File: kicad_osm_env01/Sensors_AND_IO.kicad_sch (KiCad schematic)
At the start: 64 parts, among them J4 Conn_01x08, J8 STX-3000, U10 ICS-43434, U11 HPP845E131R5, U12 MIC94073YC6, U3 VEML7700-TT

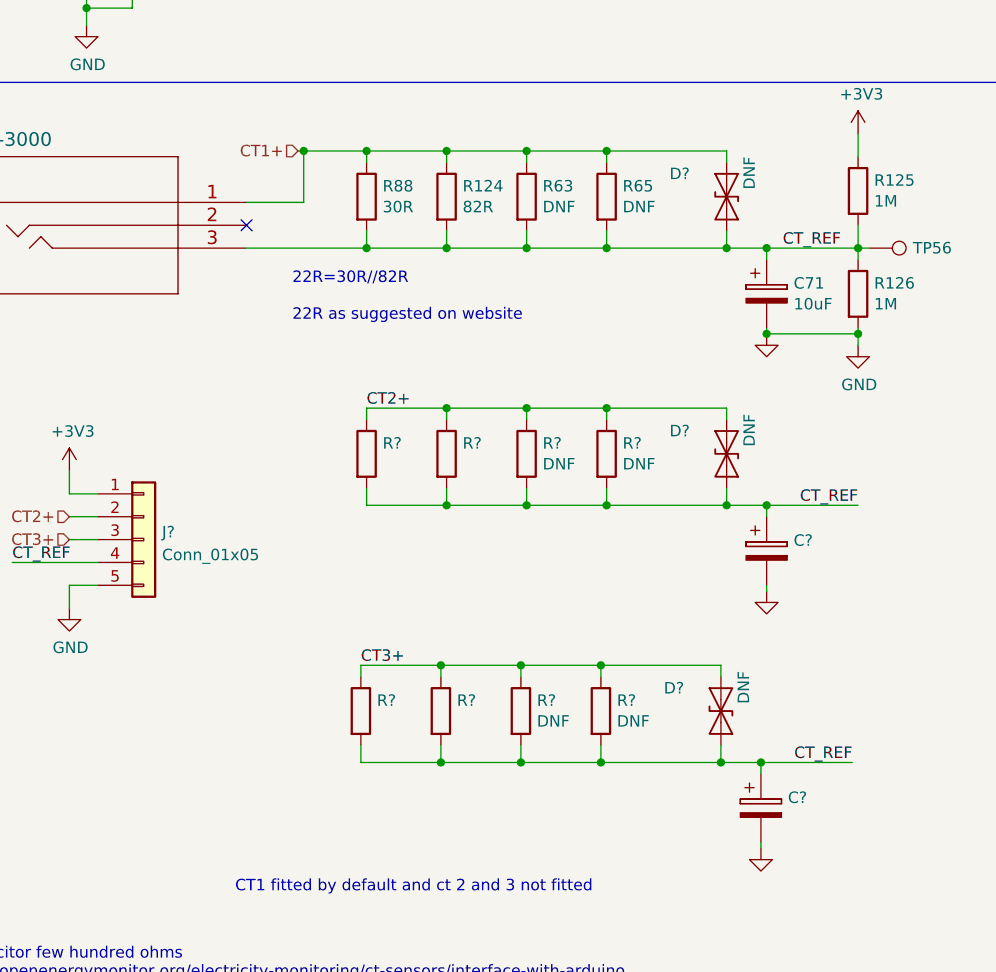
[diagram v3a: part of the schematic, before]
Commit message: added new battery charge ic u2
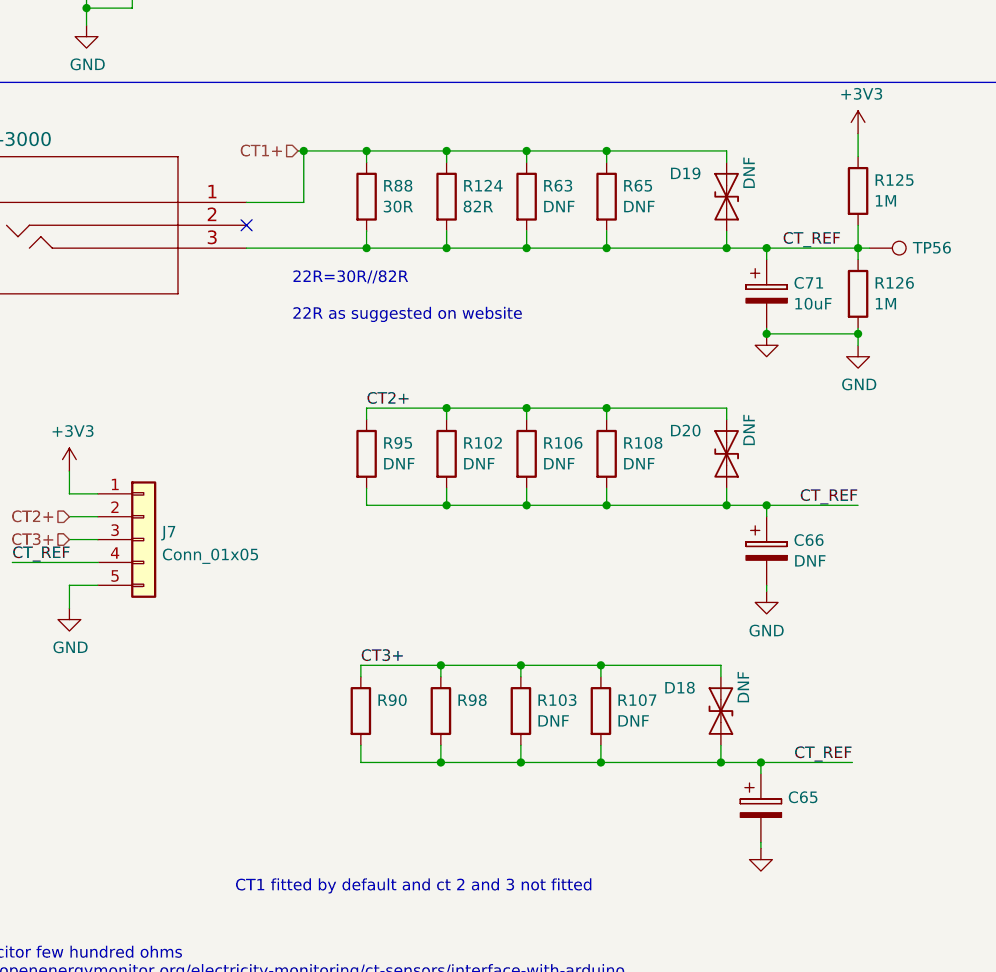
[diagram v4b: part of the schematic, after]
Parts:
- C66: renamed from C?; value (none) -> DNF
- R102, R95: renamed from R?; value (none) -> DNF
- gave numbers to parts that had none: 11
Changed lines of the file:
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@@
   (title_block
     (title "Open Smart Monitor")
-    (date "2021-09-29")
-    (rev "B")
+    (date "2022-07-01")
+    (rev "C")
     (company "Devtank LTD")
     (comment 1 "Part No: 304-010")
@@
   (symbol (lib_id "device:CP") (at 151.765 208.28 0) (unit 1)
     (in_bom yes) (on_board yes)
-    (property "Reference" "C?" (id 0) (at 154.7622 207.1116 0)
-      (effects (font (size 1.27 1.27)) (justify left))
-    )
-    (property "Value" "" (id 1) (at 154.7622 209.423 0)
+    (property "Reference" "C66" (id 0) (at 154.7622 207.1116 0)
+      (effects (font (size 1.27 1.27)) (justify left))
+    )
+    (property "Value" "DNF" (id 1) (at 154.7622 209.423 0)
       (effects (font (size 1.27 1.27)) (justify left))
     )
@@
   (symbol (lib_id "device:R") (at 107.315 197.485 0) (unit 1)
     (in_bom yes) (on_board yes)
-    (property "Reference" "R?" (id 0) (at 109.093 196.3166 0)
-      (effects (font (size 1.27 1.27)) (justify left))
-    )
-    (property "Value" "" (id 1) (at 109.093 198.628 0)
+    (property "Reference" "R95" (id 0) (at 109.093 196.3166 0)
+      (effects (font (size 1.27 1.27)) (justify left))
+    )
+    (property "Value" "DNF" (id 1) (at 109.093 198.628 0)
       (effects (font (size 1.27 1.27)) (justify left))
     )
@@
   (symbol (lib_id "device:R") (at 125.095 197.485 0) (unit 1)
     (in_bom yes) (on_board yes)
-    (property "Reference" "R?" (id 0) (at 126.873 196.3166 0)
+    (property "Reference" "R106" (id 0) (at 126.873 196.3166 0)
       (effects (font (size 1.27 1.27)) (justify left))
     )
@@
   (symbol (lib_id "device:R") (at 106.68 226.06 0) (unit 1)
     (in_bom yes) (on_board yes)
-    (property "Reference" "R?" (id 0) (at 108.458 224.8916 0)
+    (property "Reference" "R90" (id 0) (at 108.458 224.8916 0)
       (effects (font (size 1.27 1.27)) (justify left))
     )
@@
   (symbol (lib_id "device:R") (at 116.205 197.485 0) (unit 1)
     (in_bom yes) (on_board yes)
-    (property "Reference" "R?" (id 0) (at 117.983 196.3166 0)
-      (effects (font (size 1.27 1.27)) (justify left))
-    )
-    (property "Value" "" (id 1) (at 117.983 198.628 0)
+    (property "Reference" "R102" (id 0) (at 117.983 196.3166 0)
+      (effects (font (size 1.27 1.27)) (justify left))
+    )
+    (property "Value" "DNF" (id 1) (at 117.983 198.628 0)
       (effects (font (size 1.27 1.27)) (justify left))
     )
@@
   (symbol (lib_id "device:R") (at 124.46 226.06 0) (unit 1)
     (in_bom yes) (on_board yes)
-    (property "Reference" "R?" (id 0) (at 126.238 224.8916 0)
+    (property "Reference" "R103" (id 0) (at 126.238 224.8916 0)
       (effects (font (size 1.27 1.27)) (justify left))
     )
@@
   (symbol (lib_id "OSM_env01:GND") (at 151.765 212.725 0) (unit 1)
     (in_bom yes) (on_board yes) (fields_autoplaced)
-    (property "Reference" "#PWR?" (id 0) (at 151.765 219.075 0)
-      (effects (font (size 1.27 1.27)) hide)
-    )
-    (property "Value" "" (id 1) (at 151.765 217.1684 0))
+    (property "Reference" "#PWR074" (id 0) (at 151.765 219.075 0)
+      (effects (font (size 1.27 1.27)) hide)
+    )
+    (property "Value" "GND" (id 1) (at 151.765 217.1684 0))
     (property "Footprint" "" (id 2) (at 151.765 212.725 0)
       (effects (font (size 1.524 1.524)))
@@
   (symbol (lib_id "device:R") (at 133.35 226.06 0) (unit 1)
     (in_bom yes) (on_board yes)
-    (property "Reference" "R?" (id 0) (at 135.128 224.8916 0)
+    (property "Reference" "R107" (id 0) (at 135.128 224.8916 0)
       (effects (font (size 1.27 1.27)) (justify left))
     )
@@
   (symbol (lib_id "device:D_TVS") (at 147.32 197.485 270) (unit 1)
     (in_bom yes) (on_board yes)
-    (property "Reference" "D?" (id 0) (at 140.97 194.945 90)
+    (property "Reference" "D20" (id 0) (at 140.97 194.945 90)
       (effects (font (size 1.27 1.27)) (justify left))
     )
@@
   (symbol (lib_id "OSM_env01:GND") (at 151.765 184.15 0) (unit 1)
     (in_bom yes) (on_board yes) (fields_autoplaced)
-    (property "Reference" "#PWR?" (id 0) (at 151.765 190.5 0)
+    (property "Reference" "#PWR073" (id 0) (at 151.765 190.5 0)
       (effects (font (size 1.27 1.27)) hide)
     )
@@
   (symbol (lib_id "OSM_env01:GND") (at 74.295 214.63 0) (unit 1)
     (in_bom yes) (on_board yes)
-    (property "Reference" "#PWR?" (id 0) (at 74.295 220.98 0)
+    (property "Reference" "#PWR059" (id 0) (at 74.295 220.98 0)
       (effects (font (size 1.27 1.27)) hide)
     )
@@
   (symbol (lib_id "power:+3V3") (at 74.295 199.39 0) (unit 1)
     (in_bom yes) (on_board yes)
-    (property "Reference" "#PWR?" (id 0) (at 74.295 203.2 0)
+    (property "Reference" "#PWR055" (id 0) (at 74.295 203.2 0)
       (effects (font (size 1.27 1.27)) hide)
     )
@@
   (symbol (lib_id "Connector:Conn_01x05") (at 82.55 207.01 0) (unit 1)
     (in_bom yes) (on_board yes) (fields_autoplaced)
-    (property "Reference" "J?" (id 0) (at 84.582 206.1753 0)
+    (property "Reference" "J7" (id 0) (at 84.582 206.1753 0)
       (effects (font (size 1.27 1.27)) (justify left))
     )
@@
   (symbol (lib_id "device:CP") (at 151.13 236.855 0) (unit 1)
     (in_bom yes) (on_board yes)
-    (property "Reference" "C?" (id 0) (at 154.1272 235.6866 0)
+    (property "Reference" "C65" (id 0) (at 154.1272 235.6866 0)
       (effects (font (size 1.27 1.27)) (justify left))
     )
@@
   (symbol (lib_id "device:R") (at 133.985 197.485 0) (unit 1)
     (in_bom yes) (on_board yes)
-    (property "Reference" "R?" (id 0) (at 135.763 196.3166 0)
+    (property "Reference" "R108" (id 0) (at 135.763 196.3166 0)
       (effects (font (size 1.27 1.27)) (justify left))
     )
@@
   (symbol (lib_id "device:D_TVS") (at 147.32 168.91 270) (unit 1)
     (in_bom yes) (on_board yes)
-    (property "Reference" "D?" (id 0) (at 140.97 166.37 90)
+    (property "Reference" "D19" (id 0) (at 140.97 166.37 90)
       (effects (font (size 1.27 1.27)) (justify left))
     )
@@
   (symbol (lib_id "device:R") (at 115.57 226.06 0) (unit 1)
     (in_bom yes) (on_board yes)
-    (property "Reference" "R?" (id 0) (at 117.348 224.8916 0)
+    (property "Reference" "R98" (id 0) (at 117.348 224.8916 0)
       (effects (font (size 1.27 1.27)) (justify left))
     )
@@
   (symbol (lib_id "OSM_env01:GND") (at 151.13 241.3 0) (unit 1)
     (in_bom yes) (on_board yes) (fields_autoplaced)
-    (property "Reference" "#PWR?" (id 0) (at 151.13 247.65 0)
+    (property "Reference" "#PWR064" (id 0) (at 151.13 247.65 0)
       (effects (font (size 1.27 1.27)) hide)
     )
@@
   (symbol (lib_id "device:D_TVS") (at 146.685 226.06 270) (unit 1)
     (in_bom yes) (on_board yes)
-    (property "Reference" "D?" (id 0) (at 140.335 223.52 90)
-      (effects (font (size 1.27 1.27)) (justify left))
-    )
+    (property "Reference" "D18" (id 0) (at 140.335 223.52 90)
+      (effects (font (size 1.27 1.27)) (justify left))
+    )

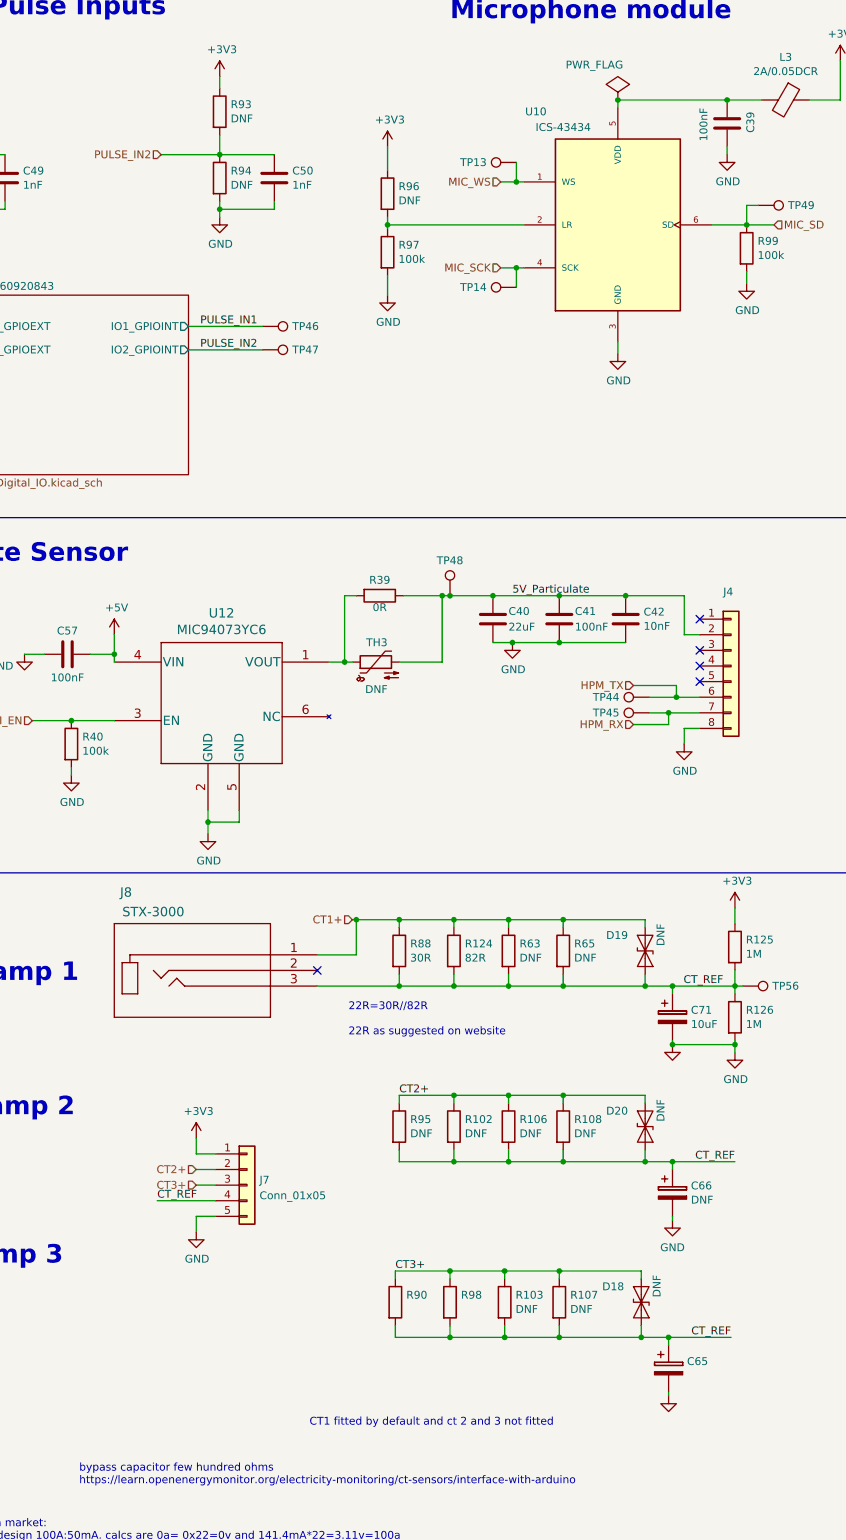
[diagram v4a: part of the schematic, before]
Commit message: updated schematics and added rs232
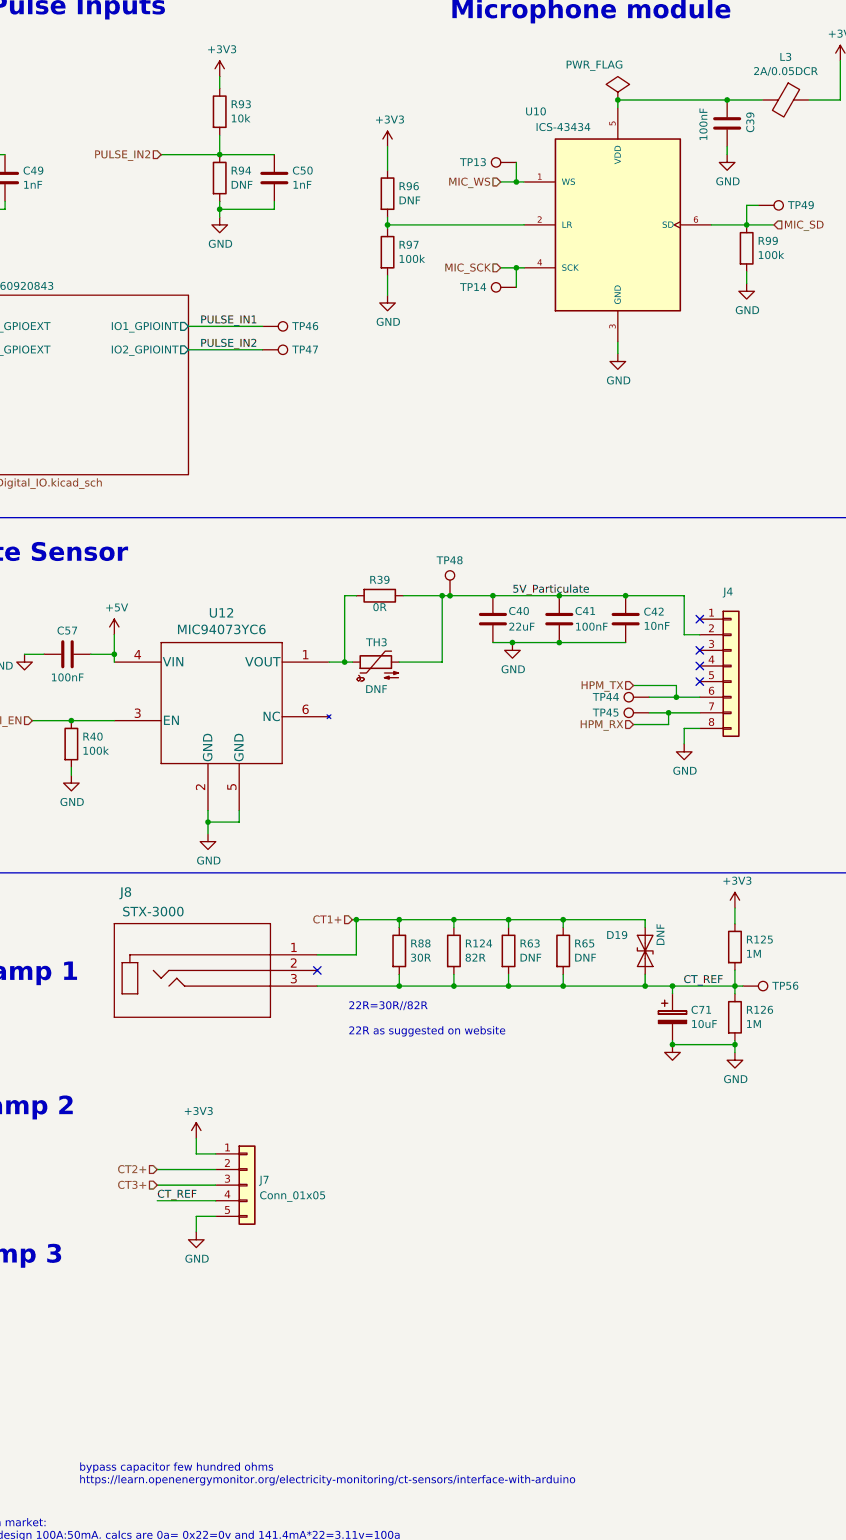
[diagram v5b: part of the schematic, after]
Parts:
- removed C65: ~, Capacitor_SMD:CP_Elec_4x5.4, symbol device:CP
- removed C66: DNF, Capacitor_SMD:CP_Elec_4x5.4, symbol device:CP
- removed D18, D20: DNF, Diode_SMD:D_SOD-123, symbol device:D_TVS
- removed R102, R103, R106, R107, R108, R95: DNF, Resistor_SMD:R_1206_3216Metric, symbol device:R
- removed R90, R98: ~, Resistor_SMD:R_1206_3216Metric, symbol device:R
- R93: value DNF -> 10k
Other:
- note removed: "CT1 fitted by default and ct 2 and 3 not fitted"

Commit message: Schematics waiting review
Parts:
- removed C45, C57: 100nF, Capacitor_SMD:C_0402_1005Metric, symbol OSM_env01-rescue:C-device-ESP32-EVB_Rev_D-rescue
- removed C49, C50: 1nF, Capacitor_SMD:C_0402_1005Metric, symbol device:C
- removed R29: 0R, Resistor_SMD:R_0603_1608Metric, symbol device:R
- removed R91, R92, R94: DNF, Resistor_SMD:R_0603_1608Metric, symbol OSM_env01-rescue:R-device-ESP32-EVB_Rev_D-rescue
- removed R93: 10k, Resistor_SMD:R_0603_1608Metric, symbol OSM_env01-rescue:R-device-ESP32-EVB_Rev_D-rescue
- removed TH3: DNF, Resistor_THT:R_Axial_DIN0617_L17.0mm_D6.0mm_P5.08mm_Vertical, symbol device:Thermistor_NTC
- added C4, C8: 100nF, Capacitor_SMD:C_0603_1608Metric, symbol device:C
- added D1, D4: DNF, Diode_SMD:D_SOD-123, symbol device:D_TVS
- added L11, L12: 2A/0.05DCR, Inductor_SMD:L_0402_1005Metric, symbol device:Ferrite_Bead
- added R41, R53, R56, R57, R61, R62, R66, R67: DNF, Resistor_SMD:R_1206_3216Metric, symbol device:R
- added R71: DNF, symbol device:R
- added TP75, TP76: Test_Point, TestPoint:TestPoint_Pad_D1.5mm, symbol OSM_env01-rescue:Test_Point-Connector-ESP32-EVB_Rev_D-rescue
- R124, R125, R126, R88: Tolerance (none) -> 0.1%
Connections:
- net +5V is gone; now on net +3V3: U12.4 (VIN)
- net +3V3: now also C4.1, L11.2, L12.2; no longer U11.5 (VDD)
- net CT2+: now also D1.1 (A1), R41.1, R56.1, R61.1, R66.1
- net CT3+: now also D4.1 (A1), R53.1, R57.1, R62.1, R67.1
- net CT_REF: now also D1.2 (A2), D4.2 (A2), R41.2, R53.2, R56.2, R57.2, R61.2, R62.2, R66.2, R67.2
- net GND: now also C4.2, C8.2, R71.2
- net at C55.1, C56.1, U3.2 (VDD): now also L12.1
- net at U11.7 (PAD): now also R71.1
- new net: C8.1, L11.1, U11.5 (VDD)
- new net PULSE1_PULLUP_EN: TP75.1
- new net PULSE2_PULLUP_EN: TP76.1
- no-connect marks 6 -> 5
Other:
- sheet sheet60920843 ports: added PULSE1_PULLUP_EN, PULSE2_PULLUP_EN, PULSE_IN1, PULSE_IN2; removed IO1_GPIOINT, IO2_GPIOINT
- note added: "CT clamp reference bypass capacitor few hundred ohms https://learn.openenergymonitor.org/electricity-monitoring/ct-sensors/interface-with-arduino Many ct cmlaps available on market: -mA output, default on this design 100A:50mA. calcs are 0a= 0x22=0v and 141.4mA*22=3.11v=100a -0-1v output - 333mv voltage output (unsure if buden resistor needed) -4-20mA - some ct clamps can provide very high voltag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"
- note removed: "Many ct cmlaps available on market: -mA output, default on this design 100A:50mA. calcs are 0a= 0x22=0v and 141.4mA*22=3.11v=100a -0-1v output - 333mv voltage output (unsure if buden resistor needed) -4-20mA - some ct clamps can provide very high voltage outputs e.g 5v and above -may need to fit tvs for current output types. yhdc internally built in -some ct clamps may need an external supply e.g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"
- note removed: "bypass capacitor few hundred ohms https://learn.openenergymonitor.org/electricity-monitoring/ct-sensors/interface-with-arduino"
- moved on the sheet: C39, C40, C41, C42, C55, C56, C71, D19, J4, J7, J8, L3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

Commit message: before fixing devtank symbol issues
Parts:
- J7: value Conn_01x05 -> (none); symbol Connector:Conn_01x05 -> Connector_Generic:Conn_01x05
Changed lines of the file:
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@@
     (pin "2")
   )
-  (symbol (lib_id "Connector:Conn_01x05") (at 288.925 186.055 0) (unit 1)
+  (symbol (lib_id "Connector_Generic:Conn_01x05") (at 288.925 186.055 0) (unit 1)
     (in_bom yes) (on_board yes) (fields_autoplaced)
     (property "Reference" "J7" (id 0) (at 290.957 185.2203 0)
       (effects (font (size 1.27 1.27)) (justify left))
     )
-    (property "Value" "Conn_01x05" (id 1) (at 290.957 187.7572 0)
+    (property "Value" "" (id 1) (at 290.957 187.7572 0)
       (effects (font (size 1.27 1.27)) (justify left))
     )
